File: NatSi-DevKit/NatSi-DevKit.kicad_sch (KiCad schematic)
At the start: 53 parts, among them J1 USB_TypeC, J2 Conn_01x22_Pin, J3 Conn_01x22_Pin, J4 MEM2067-02-180-00-A_REVB, SW1 SW_Push, SW2 SW_Push, SW3 SW_Push, U1 USBLC6-2SC6, U2 ESP32-S3-WROOM-1, U3 NCP1117-3.3_SOT223

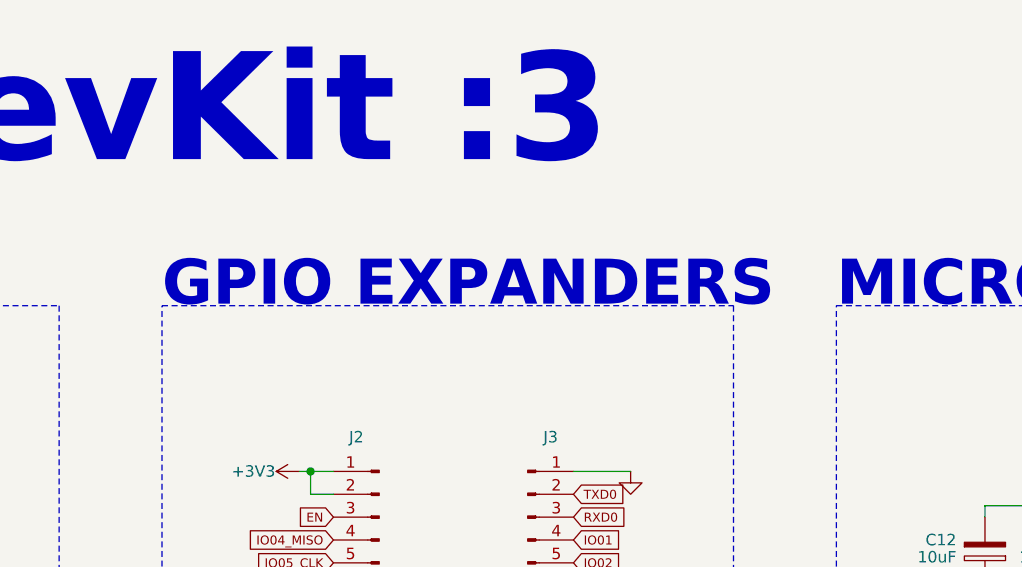
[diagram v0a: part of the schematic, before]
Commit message: text update KiCAD 9.0 switch
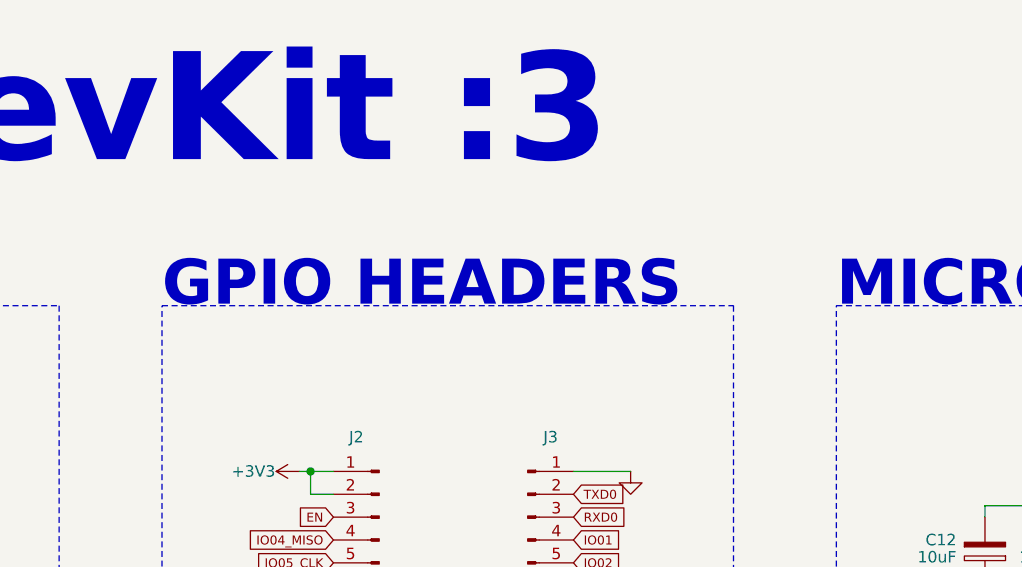
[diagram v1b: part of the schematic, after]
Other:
- note added: "GPIO HEADERS"
- note removed: "GPIO EXPANDERS"
